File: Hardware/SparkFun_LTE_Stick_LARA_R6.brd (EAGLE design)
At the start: 25.4 x 76.2 mm, 29 parts, among them IC1 SN74AVC4T774PW, IC2 SN74AVC4T774PW, J1 NANO_SIM, J2 U.FL, J3 U.FL, J7 QWIIC_RIGHT_ANGLE, U1 LARA-R6401, U2 AP7361C-33FGEUDFN-8, U3 PCA9306

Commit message: End of day commit
Extend board length
Start adding passives
Plan more routing
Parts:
- added C1, C2, C3, C4: 47pF, SparkFun-Capacitors:0603
- added C5, C6: 0.1uF, SparkFun-Capacitors:0603
- added D4: DT1042-04SO-7, SparkFun-DiscreteSemi:SOT23-6L
- added IC3: SN74AVC4T774PW, SparkFun-IC-Comms:SOP65P640X120-16N
- added JP2: JUMPER-SMT_3_2-NC_TRACE_SILK, SparkFun-Jumpers:SMT-JUMPER_3_2-NC_TRACE_SILK
- added R1, R2: 100k, SparkFun-Resistors:0603
- added R3, R4: 2.2k, SparkFun-Resistors:0603
- J5: device SparkFun-Connectors:1X08_NO_SILK -> SparkFun-Connectors:1X14_NO_SILK
- J6: device SparkFun-Connectors:1X08_NO_SILK -> SparkFun-Connectors:1X10_NO_SILK
- moved LOGO1 112.8 mm to (12.7, 91.4)
- moved D2 12.7 mm to (15.2, 80.0)
- moved D3 12.7 mm to (10.2, 80.0)
- moved E1 12.7 mm to (3.81, 86.4)
- moved E2 12.7 mm to (21.6, 86.4)
- moved H3 12.7 mm to (2.54, 80.0)
- moved H4 12.7 mm to (22.9, 80.0)
- moved J2 12.7 mm to (15.9, 83.2)
- moved J3 12.7 mm to (9.53, 83.2)
- moved U$2 12.7 mm to (12.7, 81.3)
- moved U1 12.7 mm to (12.7, 63.5)
- moved J7 12.7 mm to (5.08, 45.7)
- moved U$1 12.7 mm to (12.7, 78.0)
- moved U3 10.8 mm to (8.26, 44.5), turned to 90 degrees
- moved J1 7.62 mm to (17.8, 36.8)
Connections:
- removed net I2C_TXD: U1.35
- removed net I2S_CLK: U1.36
- removed net I2S_RXD: U1.37
- removed net I2S_WA: U1.34
- removed net VREF2: U3.7
- new net I2S_CLK_18: IC3.5, U1.36
- new net I2S_CLK_33: IC3.12, J6.7
- new net I2S_RXD_18: IC3.6, U1.37
- new net I2S_RXD_33: IC3.11, J6.6
- new net I2S_TXD_18: IC3.4, U1.35
- new net I2S_TXD_33: IC3.13, J6.8
- new net I2S_WA_18: IC3.3, U1.34
- new net I2S_WA_33: IC3.14, J6.9
- new net N$1: C6.1, R2.1, U3.7, U3.8
- new net N$2: JP2.3, R3.2
- new net N$3: JP2.1, R4.1
- new net N$4: J6.10
- new net VIN: J6.3
- net 1.8V: now also IC3.16, J6.5, R1.2
- net 3.3V: now also IC3.15, J6.4, JP2.2, R2.2
- net 5V: now also J6.2
- net GND: now also C1.2, C2.2, C3.2, C4.2, C5.2, C6.2, D4.2, D4.5, IC3.10, IC3.9, J6.1
- net SCL_33: now also R4.2
- net SDA_33: now also R3.1
- net SIM_CLK: now also C2.1, D4.4
- net SIM_DET: now also R1.1
- net SIM_IO: now also C3.1, D4.6
- net SIM_RST: now also C1.1, D4.3
- net VSIM: now also C4.1, C5.1, D4.1
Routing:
- net I2S_RXD: track 30.0 -> 0.00 mm, vias 1 -> 0
- net I2S_RXD_18: track 0.00 -> 28.4 mm, vias 0 -> 1
- net I2S_CLK_18: track 0.00 -> 27.1 mm, vias 0 -> 1
- net I2S_CLK: track 25.9 -> 0.00 mm, vias 1 -> 0
- net I2S_TXD_18: track 0.00 -> 25.8 mm, vias 0 -> 1
- net I2S_WA_18: track 0.00 -> 24.6 mm, vias 0 -> 1
- net I2C_TXD: track 21.8 -> 0.00 mm, vias 1 -> 0
- net I2S_WA: track 17.8 -> 0.00 mm, vias 1 -> 0
- net DTR/TXD2_18: track 47.6 -> 61.3 mm
- net DSR/RTS2_18: track 48.1 -> 61.9 mm
- net CTS_18: track 36.8 -> 50.6 mm
- net TXD_18: track 36.5 -> 50.2 mm
- net RXD_18: track 36.1 -> 49.9 mm
- net RTS_18: track 37.1 -> 50.9 mm
- net RI/CTS2_18: track 48.0 -> 61.7 mm
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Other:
- board size 25.4 x 76.2 mm -> 25.4 x 88.9 mm

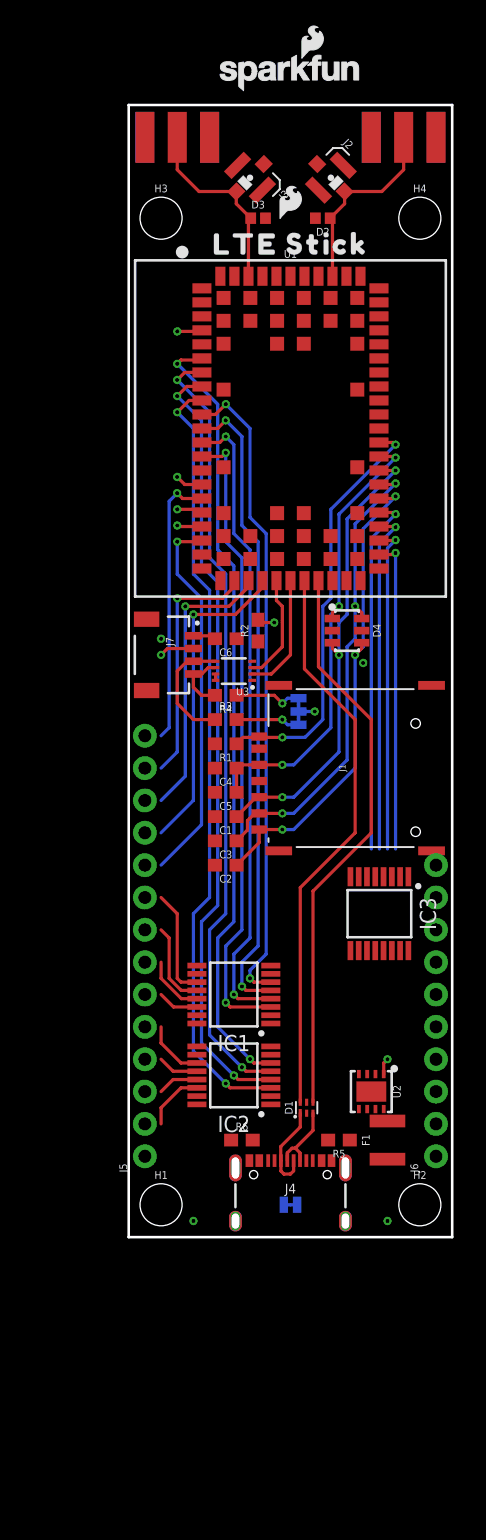
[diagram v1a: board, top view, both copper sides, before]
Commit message: Finish initial layout of v01
Change UART2, I2C, and GPIO pins to only be accessible via test points
Shrink board length to 3" again
Set initial header pinouts
Add decoupling capacitors
Route all air wires
Route USB and RF traces with proper impedance
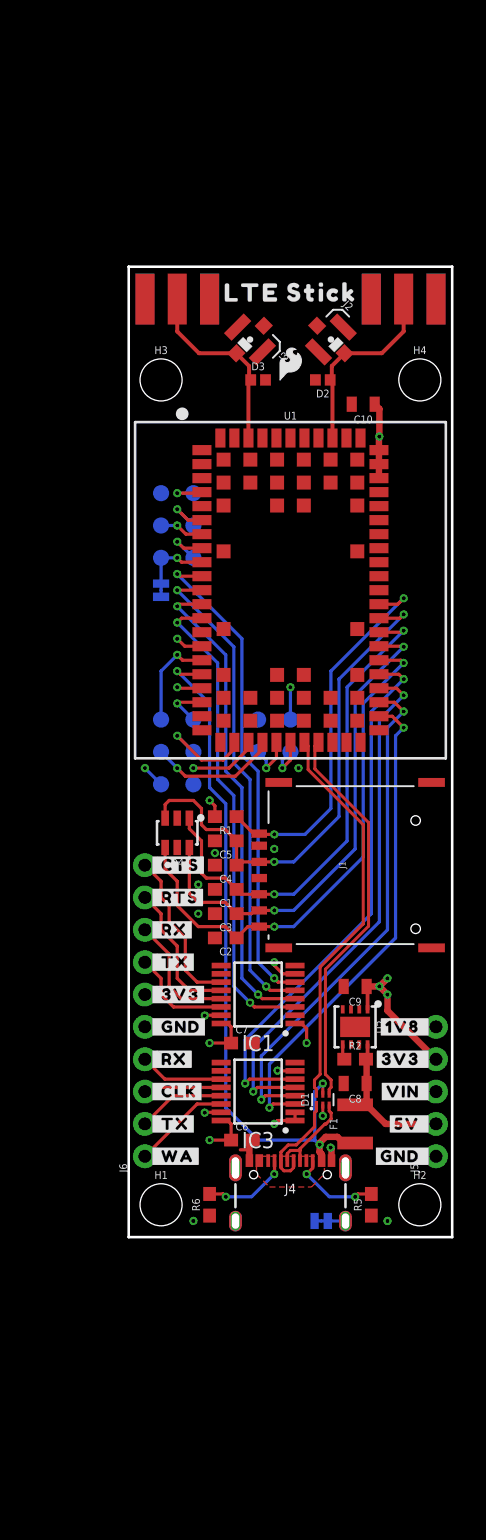
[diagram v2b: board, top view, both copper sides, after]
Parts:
- removed IC2: SN74AVC4T774PW, SparkFun-IC-Comms:SOP65P640X120-16N
- removed J7: QWIIC_RIGHT_ANGLE, SparkFun-Connectors:JST04_1MM_RA
- removed JP1: JUMPER-SMT_2_NC_TRACE_SILK, SparkFun-Jumpers:SMT-JUMPER_2_NC_TRACE_SILK
- removed JP2: JUMPER-SMT_3_2-NC_TRACE_SILK, SparkFun-Jumpers:SMT-JUMPER_3_2-NC_TRACE_SILK
- removed R3, R4: 2.2k, SparkFun-Resistors:0603
- removed U3: PCA9306, SparkFun-IC-Comms:PCA9306DC
- added C10, C8, C9: 10uF, SparkFun-Capacitors:0805
- added C7: 0.1uF, SparkFun-Capacitors:0603
- added DTR, SHLD: JUMPER-SMT_2_NC_TRACE_SILK, SparkFun-Jumpers:SMT-JUMPER_2_NC_TRACE_SILK
- added LOGO2: OSHW-LOGOM, SparkFun-Aesthetics:OSHW-LOGO-M
- added TP1, TP10, TP11, TP12, TP13, TP14, TP15, TP16, TP2, TP3, TP4, TP5, TP6, TP7, TP8, TP9: TEST-POINT3X5, SparkFun-Connectors:PAD.03X.05
- added U$10: (no value), output:#DTR#0
- added U$11: (no value), output:#VIN_#0
- added U$12, U$9: (no value), output:#3V3_#0
- added U$13: (no value), output:#1V8_#0
- added U$14: (no value), output:#_1V8#0
- added U$15, U$3: (no value), output:#_3V3#0
- added U$16: (no value), output:#_VIN#0
- added U$17: (no value), output:#_CTS#0
- added U$18: (no value), output:#_RTS#0
- added U$19, U$23: (no value), output:#_RX#0
- added U$20, U$24: (no value), output:#_TX#0
- added U$21: (no value), output:#_CLK#0
- added U$22: (no value), output:#_WA#0
- added U$25: (no value), output:LTE_STICK0
- added U$26: (no value), output:#5V_#0
- added U$27: (no value), output:#_5V#0
- added U$4, U$5: (no value), output:#_GND#0
- added U$6: (no value), output:#SHLD#0
- added U$7, U$8: (no value), output:#GND_#0
- J5: device SparkFun-Connectors:1X14_NO_SILK -> SparkFun-Connectors:1X05_NO_SILK
- U2: value AP7361C-33FGEUDFN-8 -> AP7361C-33
- moved C6 39.4 mm to (8.89, 7.62), turned to 0 degrees
- moved R2 34.5 mm to (17.8, 14.0), turned to 0 degrees
- moved J5 22.9 mm to (24.1, 6.35)
- moved J6 22.9 mm to (1.27, 6.35)
- moved LOGO1 21.6 mm to (12.7, 69.8), flipped to the bottom
- moved D4 20.7 mm to (3.81, 31.8), turned to 180 degrees
- moved IC3 16.9 mm to (10.2, 11.4), turned to 180 degrees
- moved D2 12.7 mm to (15.2, 67.3)
- moved D3 12.7 mm to (10.2, 67.3)
- moved E1 12.7 mm to (3.81, 73.7)
- moved E2 12.7 mm to (21.6, 73.7)
- moved H3 12.7 mm to (2.54, 67.3)
- moved H4 12.7 mm to (22.9, 67.3)
- moved J2 12.7 mm to (15.9, 70.5)
- moved J3 12.7 mm to (9.53, 70.5)
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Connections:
- net RXD_18 renamed TX_18
- net TXD_18 renamed RX_18
- removed net ANT_DET: U1.59
- removed net DCD/RXD2_33: IC2.13
- removed net DSR/RTS2_33: IC2.11
- removed net DTR/TXD2_33: IC2.14
- removed net N$1: C6.1, R2.1, U3.7, U3.8
- removed net N$2: JP2.3, R3.2
- removed net N$3: JP2.1, R4.1
- removed net N$4: J6.10
- removed net N$7: J4.SHLD1, J4.SHLD2, J4.SHLD3, J4.SHLD4, JP1.2
- removed net RI/CTS2_33: IC2.12
- removed net RXD_33: IC1.14
- removed net SCL_33: J7.4, R4.2, U3.6
- removed net SDA_33: J7.3, R3.1, U3.5
- removed net TXD_33: IC1.13
- new net RX_33: IC1.13, J6.8
- new net SHLD: J4.SHLD1, J4.SHLD2, J4.SHLD3, J4.SHLD4, SHLD.2
- new net TX_33: IC1.14, J6.7
- net 1.8V: now also C6.1, C7.1, IC3.1, IC3.2, IC3.7, J5.5, TP15.1, TP3.1, TP9.1; no longer IC2.1, IC2.16, IC2.7, J6.5, U3.1
- net 3.3V: now also C10.1, C9.1, J5.4, J6.6; no longer IC2.15, J6.4, J7.2, JP2.2, R2.2
- net 5V: now also C8.1, J5.2, R2.2; no longer J6.2, U1.17
- net CTS_18: now also IC1.6, U1.10; no longer IC1.5, U1.11
- net CTS_33: now also IC1.11, J6.10; no longer IC1.12
- net DCD/RXD2_18: now also TP7.1; no longer IC2.4
- net DSR/RTS2_18: now also TP5.1; no longer IC2.6
- net DTR/TXD2_18: now also DTR.2, TP8.1; no longer IC2.3
- net EN: now also R2.1
- net GND: now also C10.2, C7.2, C8.2, C9.2, DTR.1, IC3.8, J5.1, J6.5, SHLD.1, TP10.1, TP16.1, TP4.1; no longer IC2.10, IC2.2, IC2.8, IC2.9, J6.1, J7.1, JP1.1, U3.4
- net I2S_CLK_33: now also J6.3; no longer J6.7
- net I2S_RXD_33: now also J6.4; no longer J6.6
- net I2S_TXD_33: now also J6.2; no longer J6.8
- net I2S_WA_33: now also J6.1; no longer J6.9
- net IO1_18: now also TP11.1
- net IO2_18: now also TP12.1
- net IO4_18: now also TP13.1
- net IO6_18: now also TP14.1
- net RI/CTS2_18: now also TP6.1; no longer IC2.5
- net RTS_18: now also IC1.5, U1.11; no longer IC1.6, U1.10
- net RTS_33: now also IC1.12, J6.9; no longer IC1.11
- net SCL_18: now also TP2.1; no longer U3.2
- net SDA_18: now also TP1.1; no longer U3.3
- net SIM_RST: now also D4.1; no longer D4.3
- net VIN: now also J5.3; no longer J6.3
- net VSIM: now also D4.3; no longer D4.1
- net V_USB: now also U1.17
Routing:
- net RI/CTS2_18: track 61.7 -> 3.49 mm, vias 2 -> 1
- net DSR/RTS2_18: track 61.9 -> 4.09 mm, vias 2 -> 1
- net DCD/RXD2_18: track 61.5 -> 3.95 mm, vias 2 -> 1
- net V_USB: track 0.00 -> 56.7 mm, vias 0 -> 3
- net DTR/TXD2_18: track 61.3 -> 5.37 mm, vias 2 -> 1
- net 1.8V: track 1.97 -> 38.1 mm, vias 1 -> 10
- net IO6_18: track 29.5 -> 3.77 mm
- net IO3_18: track 22.1 -> 5.45 mm
- net IO4_18: track 25.0 -> 10.2 mm
- net I2S_RXD_18: track 28.4 -> 43.1 mm, vias 1 -> 2
- net I2S_CLK_18: track 27.1 -> 41.6 mm, vias 1 -> 2
- net I2S_TXD_18: track 25.8 -> 40.1 mm, vias 1 -> 2
- net I2S_WA_18: track 24.6 -> 38.7 mm, vias 1 -> 2
- net IO1_18: track 21.7 -> 7.72 mm
- net USB_P: track 44.6 -> 31.1 mm
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- added copper zone on layer 15, net 1.8V
- added copper zone on layer 2, net SHLD
- added copper zone on layer 1, net V_USB
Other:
- board size 25.4 x 88.9 mm -> 25.4 x 76.2 mm

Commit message: Design review updates
Extend board length to 3.25"
Remove u.FL connectors
Rename UART pins to match u-blox naming
Add Reset and PWR_ON buttons and header pads
Add power LEDs
Add fiducials
Add 100uF bulk capacitor
Add decoupling capacitors for LARA-R6
Move SIM ESD diode
Move GPIO4 test point
Connect GPIO3 to test point
Add pulldown to RTS
Connect DTR to GND via jumper
Nudge SMA connectors to align with board edge
Add Buzzard labels
Add version number in copper
Add layer numbers in copper
Add GND vias
Add measures
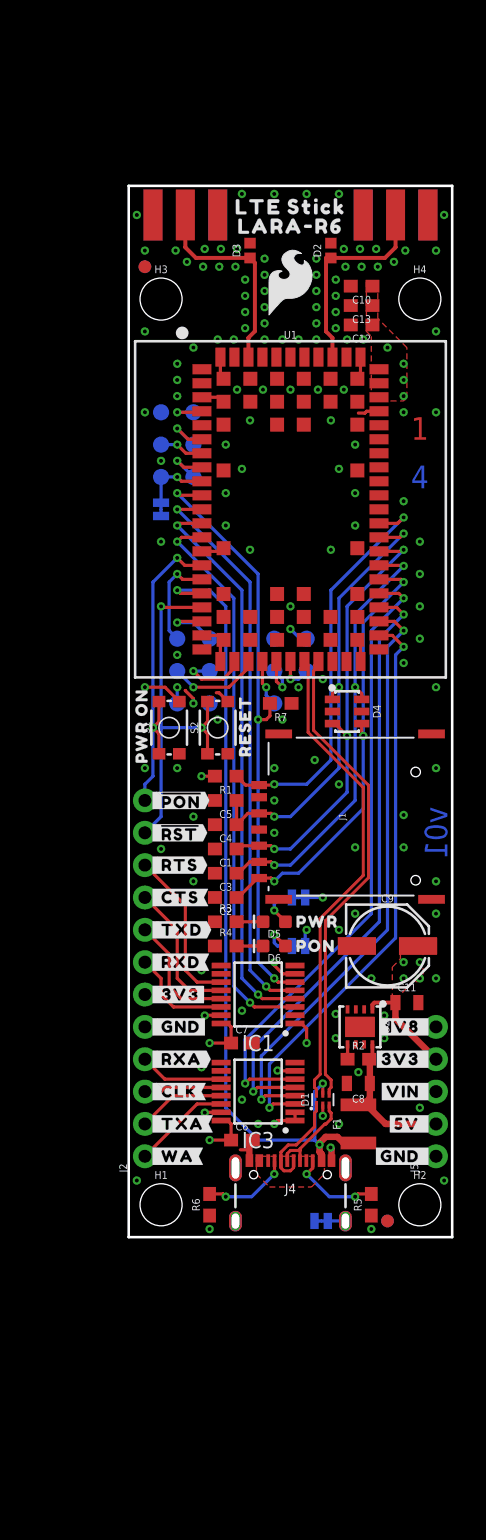
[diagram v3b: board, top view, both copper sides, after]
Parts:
- removed J3: U.FL, SparkFun-Connectors:U.FL
- removed J6: (no value), SparkFun-Connectors:1X10_NO_SILK
- added C11: 10uF, SparkFun-Capacitors:0805
- added C12: 15pF, SparkFun-Capacitors:0603
- added C13: 68pF, SparkFun-Capacitors:0603
- added D5, D6: (no value), SparkFun-LED:LED-0603
- added FD1, FD2, FD3, FD4: FIDUCIAL1X2, SparkFun-Aesthetics:FIDUCIAL-1X2
- added PON, PWR: JUMPER-SMT_2_NC_TRACE_SILK, SparkFun-Jumpers:SMT-JUMPER_2_NC_TRACE_SILK
- added R3: 4.7k, SparkFun-Resistors:0603
- added R4: 220, SparkFun-Resistors:0603
- added R7: 100k, SparkFun-Resistors:0603
- added S1, S2: MOMENTARY-SWITCH-SPST-SMD-4.6X2.8MM, SparkFun-Switches:TACTILE_SWITCH_SMD_4.6X2.8MM
- added TP17: TEST-POINT3X5, SparkFun-Connectors:PAD.03X.05
- added U$28: (no value), output:PWR0
- added U$29: (no value), output:#_#PON##0
- added U$30: (no value), output:RESET0
- added U$31, U$35: (no value), output:LARA#R60
- added U$32: (no value), output:#_RXA#0
- added U$33: (no value), output:#_#RST##0
- added U$34: (no value), output:PWR_ON0
- added U$36: (no value), output:#PWR#0
- added U$37: (no value), output:PON0
- added U$38: (no value), output:##PWR_ON#_#0
- added U$39: (no value), output:#PON#0
- added U$40: (no value), output:#_TXA#0
- added U$41: (no value), output:#_TXD#0
- added U$42: (no value), output:#_RXD#0
- added U$43: (no value), output:#CLK_#0
- added U$44: (no value), output:#WA_#0
- added U$45: (no value), output:#RTS_#0
- added U$46: (no value), output:#CTS_#0
- added U$47: (no value), output:##RESET#_#0
- added U$48: (no value), output:UART0
- added U$49: (no value), output:I2S0
- C10: value 10uF -> 0.1uF; device SparkFun-Capacitors:0805 -> SparkFun-Capacitors:0603
- C9: value 10uF -> 100uF; device SparkFun-Capacitors:0805 -> SparkFun-Capacitors:PANASONIC_D
- J2: value U.FL -> (none); device SparkFun-Connectors:U.FL -> SparkFun-Connectors:1X12_NO_SILK
- U$19: device output:#_RX#0 -> output:#RXD_#0
- U$2: device SparkFun-Aesthetics:SFE_LOGO_FLAME_.1 -> SparkFun-Aesthetics:SFE_LOGO_FLAME_.2
- U$20: device output:#_TX#0 -> output:#TXD_#0
- U$23: device output:#_RX#0 -> output:#RXA_#0
- U$24: device output:#_TX#0 -> output:#TXA_#0
- moved J2 65.8 mm to (1.27, 6.35), turned to 90 degrees
- moved FRAME1 28.5 mm to (-10.2, -25.4)
- moved D4 16.4 mm to (17.1, 41.3), turned to 270 degrees
- moved D2 10.2 mm to (15.9, 77.5), turned to 90 degrees
- moved D3 10.2 mm to (9.53, 77.5), turned to 90 degrees
- moved C10 9.27 mm to (18.3, 74.7)
- moved LOGO1 7.62 mm to (12.7, 62.2)
- moved LOGO2 7.62 mm to (12.7, 53.3)
- moved U$10 7.27 mm to (3.17, 57.1), turned to 0 degrees
- moved U$25 6.86 mm to (12.7, 59.7)
- moved U$1 6.73 mm to (12.7, 80.9)
- moved E1 6.63 mm to (4.45, 80.3)
- moved E2 6.63 mm to (21.0, 80.3)
- moved TP1 6.48 mm to (11.4, 44.5)
- moved TP11 6.48 mm to (3.81, 47.0)
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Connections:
- net I2S_RXD_18 renamed I2S_RXA_18
- net I2S_TXD_18 renamed I2S_TXA_18
- net RX_18 renamed TXD_18
- net TX_18 renamed RXD_18
- removed net I2S_RXD_33: IC3.11, J6.4
- removed net I2S_TXD_33: IC3.13, J6.2
- removed net RX_33: IC1.13, J6.8
- removed net TX_33: IC1.14, J6.7
- new net I2S_RXA_33: IC3.11, J2.4
- new net I2S_TXA_33: IC3.13, J2.2
- new net N$1: D5.C, R3.2
- new net N$2: D5.A, PWR.1
- new net N$3: D6.A, PON.1
- new net N$4: D6.C, R4.2
- new net RXD_33: IC1.14, J2.7
- new net TXD_33: IC1.13, J2.8
- net !RESET!: now also J2.11, S2.3, S2.4
- net 1.8V: now also PON.2
- net 3.3V: now also C11.1, C12.1, C13.1, C9.+, J2.6, PWR.2; no longer C9.1, J6.6
- net ANT1: no longer J2.FEED
- net ANT2: no longer J3.FEED
- net CTS_18: now also IC1.5, U1.11; no longer IC1.6, U1.10
- net CTS_33: now also IC1.12, J2.9; no longer IC1.11, J6.10
- net GND: now also C11.2, C12.2, C13.2, C9.-, J2.5, R3.1, R4.1, R7.1, S1.1, S1.2, S2.1, S2.2; no longer C9.2, J2.1, J2.2, J3.1, J3.2, J6.5
- net I2S_CLK_33: now also J2.3; no longer J6.3
- net I2S_WA_33: now also J2.1; no longer J6.1
- net IO3_18: now also TP13.1
- net IO4_18: now also TP17.1; no longer TP13.1
- net PWR_ON: now also J2.12, S1.3, S1.4
- net RTS_18: now also IC1.6, R7.2, U1.10; no longer IC1.5, U1.11
- net RTS_33: now also IC1.11, J2.10; no longer IC1.12, J6.9
- net SIM_RST: now also D4.3; no longer D4.1
- net VSIM: now also D4.1; no longer D4.3
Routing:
- net !RESET!: track 1.97 -> 29.2 mm, vias 1 -> 2
- net PWR_ON: track 2.18 -> 26.8 mm, vias 1 -> 2
- net GND: track 5.20 -> 24.4 mm, vias 9 -> 131
- net TXD_33: track 0.00 -> 9.72 mm
- net RX_33: track 9.72 -> 0.00 mm
- net RTS_18: track 38.3 -> 47.0 mm, vias 2 -> 3
- net TX_33: track 8.19 -> 0.00 mm
- net RXD_33: track 0.00 -> 8.19 mm
- net V_USB: track 56.7 -> 64.8 mm
- net 3.3V: track 19.9 -> 12.0 mm, vias 6 -> 11
- net I2S_TXD_33: track 6.91 -> 0.00 mm
- net I2S_TXA_33: track 0.00 -> 6.91 mm
- net SIM_CLK: track 41.8 -> 35.2 mm, vias 2 -> 3
- net I2S_RXD_33: track 6.64 -> 0.00 mm
- net I2S_RXA_33: track 0.00 -> 6.64 mm
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- added copper zone on layer 1, net 3.3V
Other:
- board size 25.4 x 76.2 mm -> 25.4 x 82.5 mm
- board text added: "1"
- board text added: "2"
- board text added: "3"
- board text added: "4"
- board text added: "Dryw Wade"
- board text added: "Units: inches"
- board text added: "v01"
